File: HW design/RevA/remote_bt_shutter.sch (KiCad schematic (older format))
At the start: 36 parts

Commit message: More work on the PCB logic
More work, added two switches switch and a LED.
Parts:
- added D?: LED, ~, symbol LED
- added P?: CONN_2, symbol CONN_2
- added P?: MODE_SW, symbol CONN_2
- added P?: SW3, symbol CONN_2
- added R? (x2): 10k, ~, symbol R
- added R?: 200, ~, symbol R
- P?: value PWR_SW -> BATT_CONN
- P?: value MODE_SW -> SW2
- P?: value SHUTTER_SW -> SW1
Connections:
- wire segments 147 -> 218

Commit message: Finished PCB logic design
PCB logic design finished.
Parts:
- added D?: TBD, ~, symbol DIODESCH
- added P?: TP_BT_RX, ~, symbol TST
- added P?: TP_BT_TX, ~, symbol TST
- added R? (x2): R, ~, symbol R
- P?: value CONN_2 -> PWR_SW
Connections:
- net labels added: LOW_BATT_IND
- wire segments 218 -> 189
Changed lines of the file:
@@
 Sheet 1 1
 Title ""
-Date "14 jun 2015"
+Date "20 jun 2015"
 Rev ""
 Comp ""
@@
 P 10975 6075
 F 0 "P?" V 10925 6075 40  0000 C CNN
-F 1 "CONN_2" V 11025 6075 40  0000 C CNN
+F 1 "PWR_SW" V 11025 6075 40  0000 C CNN
 F 2 "" H 10975 6075 60  0000 C CNN
 F 3 "" H 10975 6075 60  0000 C CNN
@@
 	3650 4650 3050 4650
 Wire Wire Line
-	3050 4200 3050 4650
-Wire Wire Line
-	3050 4650 3050 4800
+	3050 4200 3050 4800
 Wire Wire Line
 	3050 4200 2800 4200
@@
 	3200 5850 2650 5850
 Wire Wire Line
-	2650 5300 2650 5850
-Wire Wire Line
-	2650 5850 2650 6300
+	2650 5300 2650 6300
 Wire Wire Line
 	2650 5300 1700 5300
@@
 	6375 1050 6650 1050
 Wire Wire Line
-	6650 1150 1775 1150
+	1775 1150 6650 1150
 Wire Wire Line
 	1775 1150 1775 2550
@@
 	6500 2250 6500 3550
 Wire Wire Line
-	5000 3550 6225 3550
-Wire Wire Line
-	6225 3550 6500 3550
-Wire Wire Line
-	6500 3550 6975 3550
-Wire Wire Line
-	6975 3550 8150 3550
+	5000 3550 8150 3550
 Wire Wire Line
 	6225 3550 6225 3825
@@
 Connection ~ 6500 3550
 Wire Wire Line
-	900  1650 2350 1650
-Wire Wire Line
-	2350 1650 2600 1650
+	900  1650 2600 1650
 Wire Wire Line
 	2550 1350 2350 1350
 Connection ~ 2350 1350
 Wire Wire Line
-	2750 1350 2825 1350
-Wire Wire Line
-	2825 1350 4850 1350
-Wire Wire Line
-	4850 1350 5000 1350
-Wire Wire Line
-	5000 1350 5700 1350
+	2750 1350 5700 1350
 Wire Wire Line
 	4850 1350 4850 1650
@@
 	4850 1650 4700 1650
 Wire Wire Line
-	2350 950  2350 1350
-Wire Wire Line
-	2350 1350 2350 1650
-Wire Wire Line
-	2350 950  4325 950
-Wire Wire Line
-	4325 950  5150 950
-Wire Wire Line
-	5150 950  5375 950
-Wire Wire Line
-	5375 950  5800 950
-Wire Wire Line
-	5800 950  6000 950
-Wire Wire Line
-	6000 950  6125 950
+	2350 950  2350 1650
+Wire Wire Line
+	2350 950  6125 950
 Wire Wire Line
 	4325 950  4325 800
@@
 Connection ~ 5000 1350
 Wire Wire Line
-	5700 2150 6000 2150
-Wire Wire Line
-	6000 2150 6650 2150
+	5700 2150 6650 2150
 Wire Wire Line
 	5700 1350 5700 1950
@@
 	5000 3550 5000 1350
 Wire Wire Line
-	5150 1525 5150 2050
-Wire Wire Line
-	5150 2050 5150 5800
+	5150 1525 5150 5800
 Wire Wire Line
 	5150 2050 4700 2050
 Wire Wire Line
-	5375 1525 5375 2150
-Wire Wire Line
-	5375 2150 5375 5625
+	5375 1525 5375 5625
 Wire Wire Line
 	5375 2150 4700 2150
@@
 	5825 6325 5825 6075
 Wire Wire Line
-	4975 6075 5825 6075
-Wire Wire Line
-	5825 6075 6975 6075
-Wire Wire Line
-	6975 6075 7625 6075
-Wire Wire Line
-	6975 3550 6975 4350
-Wire Wire Line
-	6975 4350 6975 4700
-Wire Wire Line
-	6975 4700 6975 6075
-Wire Wire Line
-	6975 6075 6975 6325
+	4975 6075 7625 6075
+Wire Wire Line
+	6975 3550 6975 6325
 Connection ~ 6975 3550
 Connection ~ 6975 6075
@@
 	4875 2350 4700 2350
 Wire Wire Line
-	900  1150 900  1350
-Wire Wire Line
-	900  1350 900  1650
+	900  1150 900  1650
 Connection ~ 2350 1650
 Wire Wire Line
@@
 	2825 1500 1000 1500
 Wire Wire Line
-	1000 1150 1000 1500
-Wire Wire Line
-	1000 1500 1000 2350
+	1000 1150 1000 2350
 Connection ~ 2825 1350
 Wire Wire Line
@@
 	1175 1950 600  1950
 Wire Wire Line
-	600  1850 600  1950
-Wire Wire Line
-	600  1950 600  2050
+	600  1850 600  2050
 Connection ~ 600  1950
 Wire Wire Line
@@
 	800  1800 1575 1800
 Wire Wire Line
-	1575 1800 1575 1950
+	1575 1800 1575 2125
 Wire Wire Line
 	600  1350 900  1350
 Connection ~ 900  1350
 Wire Wire Line
-	600  2250 600  2350
-Wire Wire Line
-	600  2350 600  3650
+	600  2250 600  3650
 Wire Wire Line
 	1000 2350 600  2350
 Connection ~ 1000 1500
 Wire Wire Line
-	850  2650 850  3000
-Wire Wire Line
-	850  3000 850  3350
-Wire Wire Line
-	1450 2775 1450 3000
-Wire Wire Line
-	1450 3000 1450 3350
+	850  2775 850  3350
+Wire Wire Line
+	1450 2775 1450 3350
 Wire Wire Line
 	1450 3650 1450 3550
 Wire Wire Line
-	600  3650 850  3650
-Wire Wire Line
-	850  3650 1450 3650
+	600  3650 1450 3650
 Wire Wire Line
 	850  3650 850  3550
@@
 	1850 1750 1850 2200
 Wire Wire Line
-	1850 2200 1150 2200
-Wire Wire Line
-	1150 2200 1150 2650
-Wire Wire Line
-	1150 2650 850  2650
+	1850 2200 1350 2200
+Wire Wire Line
+	1350 2200 1350 2775
+Wire Wire Line
+	1350 2775 850  2775
 Connection ~ 850  3000
 Wire Wire Line
-	10300 5200 10350 5200
-Wire Wire Line
-	10350 5200 10550 5200
+	10300 5200 10550 5200
 Wire Wire Line
 	10350 5200 10350 4800
@@
 	9100 5500 8250 5500
 Wire Wire Line
-	8250 4300 8250 5500
-Wire Wire Line
-	8250 5500 8250 6350
-Wire Wire Line
-	8150 5600 9000 5600
-Wire Wire Line
-	9000 5600 9100 5600
+	8250 4300 8250 6350
+Wire Wire Line
+	8150 5600 9100 5600
 Connection ~ 10350 5200
 Wire Wire Line
-	8250 6350 8350 6350
-Wire Wire Line
-	8350 6350 10350 6350
-Wire Wire Line
-	10350 6350 10400 6350
+	8250 6350 10400 6350
 Wire Wire Line
 	9100 5900 9000 5900
@@
 	10350 6350 10350 6450
 Wire Wire Line
-	10550 4700 10550 5200
-Wire Wire Line
-	10550 5200 10550 5975
+	10550 4700 10550 5975
 Wire Wire Line
 	10550 6175 10550 6450
-Wire Wire Line
-	10300 5500 10400 5500
-Wire Wire Line
-	10400 5500 10400 6350
-Connection ~ 10350 6350
 Connection ~ 10550 5200
 Wire Wire Line
-	8250 4300 9750 4300
-Wire Wire Line
-	9750 4300 10550 4300
+	8250 4300 10550 4300
 Connection ~ 8250 5500
 Wire Wire Line
 	10550 4700 10750 4700
 Wire Wire Line
-	10300 5300 10750 5300
-Wire Wire Line
-	10750 5300 11050 5300
+	10300 5300 11050 5300
 Wire Wire Line
 	11050 5300 11050 4000
@@
 Connection ~ 10750 5300
 Wire Wire Line
-	10300 5600 10300 6100
-Wire Wire Line
-	10300 6100 9950 6100
+	10300 6100 10300 5600
+Wire Wire Line
+	9950 6100 10300 6100
 Wire Wire Line
 	9450 6100 9250 6100
@@
 	8150 5600 8150 4000
 Wire Wire Line
-	8150 4000 10150 4000
-Wire Wire Line
-	10150 4000 10550 4000
-Wire Wire Line
-	10150 3525 10150 3775
-Wire Wire Line
-	10150 3775 10150 4000
+	8150 4000 10550 4000
+Wire Wire Line
+	10150 3525 10150 4000
 Connection ~ 10150 3775
 Connection ~ 10150 4000
@@
 	8350 5300 8350 5900
 Wire Wire Line
-	8350 6100 8350 6350
-Wire Wire Line
-	8350 6350 8350 6750
+	8350 6100 8350 6750
 Connection ~ 8350 6350
 Wire Wire Line
@@
 	5850 4075 5850 2250
 Wire Wire Line
-	4700 2250 5850 2250
-Wire Wire Line
-	5850 2250 5900 2250
+	4700 2250 5900 2250
 Wire Wire Line
 	5800 1525 5800 1775
@@
 	7425 2975 7425 6325
 Wire Wire Line
-	5675 2975 6125 2975
-Wire Wire Line
-	6125 2975 7425 2975
+	5675 2975 7425 2975
 Wire Wire Line
 	5675 2975 5675 2550
@@
 Wire Wire Line
 	4600 4700 5600 4700
+Wire Wire Line
+	1450 2775 1600 2775
+Wire Wire Line
+	1600 2775 1600 2275
+Connection ~ 1600 2275
+$Comp
+L TST P?
+U 1 1 55856C5B
+P 6275 875
+F 0 "P?" H 6275 1175 40  0000 C CNN
+F 1 "TP_BT_RX" H 6275 1125 30  0000 C CNN
+F 2 "~" H 6275 875 60  0000 C CNN
+F 3 "~" H 6275 875 60  0000 C CNN
+	1    6275 875
+	1    0    0    -1
+$EndComp
+$Comp
+L TST P?
+U 1 1 55856C6A
+P 6500 875
+F 0 "P?" H 6500 1175 40  0000 C CNN
+F 1 "TP_BT_TX" H 6500 1125 30  0000 C CNN
+F 2 "~" H 6500 875 60  0000 C CNN
+F 3 "~" H 6500 875 60  0000 C CNN
+	1    6500 875
+	1    0    0    -1
+$EndComp
+Wire Wire Line
+	6500 875  6500 1050
+Connection ~ 6500 1050
+Wire Wire Line
+	6275 875  6275 1150
+Connection ~ 6275 1150
+Wire Wire Line
+	9100 6100 9100 6350
+Connection ~ 9100 6350
+Connection ~ 10350 6350
+Wire Wire Line
+	10400 5500 10400 5650
+Wire Wire Line
+	10400 6350 10400 6150
+Wire Wire Line
+	10300 5500 10650 5500
+$Comp
+L R R?
+U 1 1 5585745E
+P 10400 5900
+F 0 "R?" V 10480 5900 40  0000 C CNN
+F 1 "R" V 10407 5901 40  0000 C CNN
+F 2 "~" V 10330 5900 30  0000 C CNN
+F 3 "~" H 10400 5900 30  0000 C CNN
+	1    10400 5900
+	1    0    0    -1
+$EndComp
+$Comp
+L R R?
+U 1 1 5585766C
+P 10900 5500
+F 0 "R?" V 10980 5500 40  0000 C CNN
+F 1 "R" V 10907 5501 40  0000 C CNN
+F 2 "~" V 10830 5500 30  0000 C CNN
+F 3 "~" H 10900 5500 30  0000 C CNN
+	1    10900 5500
+	0    1    1    0
+$EndComp
+Connection ~ 10400 5500
+Wire Wire Line
+	11150 5500 11150 5650
+Wire Wire Line
+	11150 5650 10550 5650
+Connection ~ 10550 5650
+Text Label 9500 6750 2    60   ~ 0
+LOW_BATT_IND
+Wire Wire Line
+	10100 6100 10100 6750
+Wire Wire Line
+	10100 6750 9500 6750
+Connection ~ 10100 6100
+$Comp
+L DIODESCH D?
+U 1 1 55857A3F
+P 1175 2325
+F 0 "D?" H 1175 2425 40  0000 C CNN
+F 1 "TBD" H 1175 2225 40  0000 C CNN
+F 2 "~" H 1175 2325 60  0000 C CNN
+F 3 "~" H 1175 2325 60  0000 C CNN
+	1    1175 2325
+	0    -1   -1   0
+$EndComp
+Wire Wire Line
+	1575 2125 1175 2125
+Connection ~ 1575 1950
+Wire Wire Line
+	1175 2525 700  2525
+Wire Wire Line
+	700  2525 700  4050
+Text Label 850  4050 0    60   ~ 0
+LOW_BATT_IND
+Wire Wire Line
+	700  4050 850  4050
 $EndSCHEMATC

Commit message: Netlist before the new footprints
Parts netlist done, other than for the parts that need footprints
created.
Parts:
- removed P?: NIKON_CONN4, symbol CONN_4
- added K1: NIKON_CONN, symbol CONN_3
- gave numbers to parts that had none: 47
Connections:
- wire segments 189 -> 191
- no-connect marks 29 -> 28

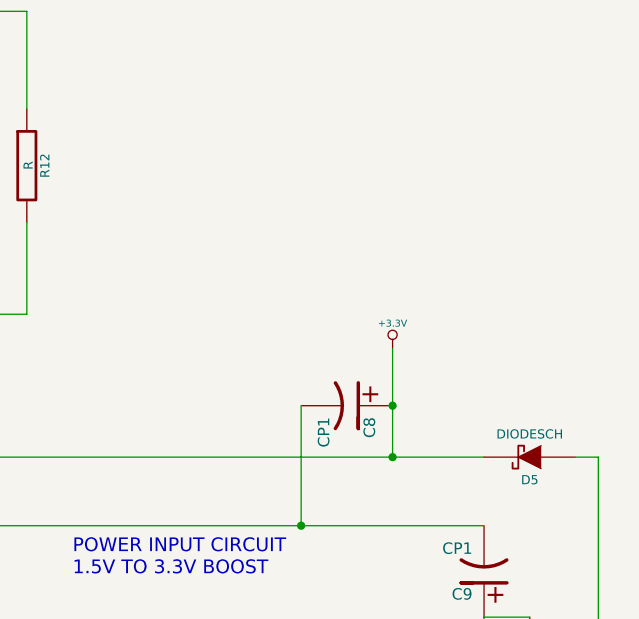
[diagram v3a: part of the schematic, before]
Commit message: Added a diode from power circuit
To be on the safe side, added a diode to protect the power circuit from any current from the ICSP prommer. Is actually a shorted connector which can be in time of catastrophy have the trace cut and diode added.
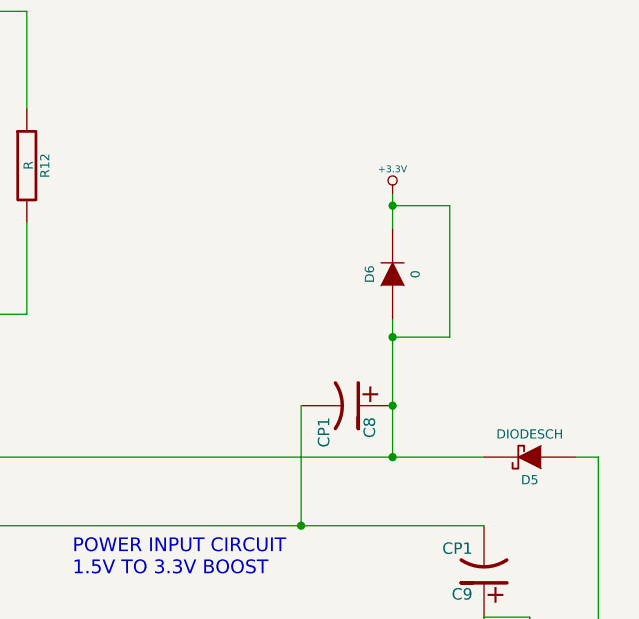
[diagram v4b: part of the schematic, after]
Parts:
- added D6: 0, ~, symbol DIODE
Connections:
- wire segments 191 -> 195
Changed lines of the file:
@@
 Sheet 1 1
 Title ""
-Date "20 jun 2015"
+Date "22 jun 2015"
 Rev ""
 Comp ""
@@
 L +3.3V #PWR04
 U 1 1 53E65AA7
-P 10150 3525
-F 0 "#PWR04" H 10150 3485 30  0001 C CNN
-F 1 "+3.3V" H 10150 3635 30  0000 C CNN
-F 2 "" H 10150 3525 60  0000 C CNN
-F 3 "" H 10150 3525 60  0000 C CNN
-	1    10150 3525
+P 10150 2850
+F 0 "#PWR04" H 10150 2810 30  0001 C CNN
+F 1 "+3.3V" H 10150 2960 30  0000 C CNN
+F 2 "" H 10150 2850 60  0000 C CNN
+F 3 "" H 10150 2850 60  0000 C CNN
+	1    10150 2850
 	1    0    0    -1
 $EndComp
@@
 	8150 4000 10550 4000
 Wire Wire Line
-	10150 3525 10150 4000
+	10150 3400 10150 4000
 Connection ~ 10150 3775
 Connection ~ 10150 4000
@@
 	0    1    1    0
 $EndComp
+$Comp
+L DIODE D6
+U 1 1 55886569
+P 10150 3200
+F 0 "D6" H 10150 3300 40  0000 C CNN
+F 1 "0" H 10150 3100 40  0000 C CNN
+F 2 "~" H 10150 3200 60  0000 C CNN
+F 3 "~" H 10150 3200 60  0000 C CNN
+	1    10150 3200
+	0    -1   -1   0
+$EndComp
+Wire Wire Line
+	10150 3000 10150 2850
+Wire Wire Line
+	10150 3475 10400 3475
+Wire Wire Line
+	10400 3475 10400 2900
+Wire Wire Line
+	10400 2900 10150 2900
+Connection ~ 10150 2900
+Connection ~ 10150 3475
 $EndSCHEMATC
